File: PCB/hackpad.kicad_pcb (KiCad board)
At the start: 2 copper layers, 67 x 62 mm, 6 parts, among them SW1 SW_Push, SW2 SW_Push, SW3 SW_Push, SW4 SW_Push, U1 MOUDLE-SEEEDUINO-XIAO

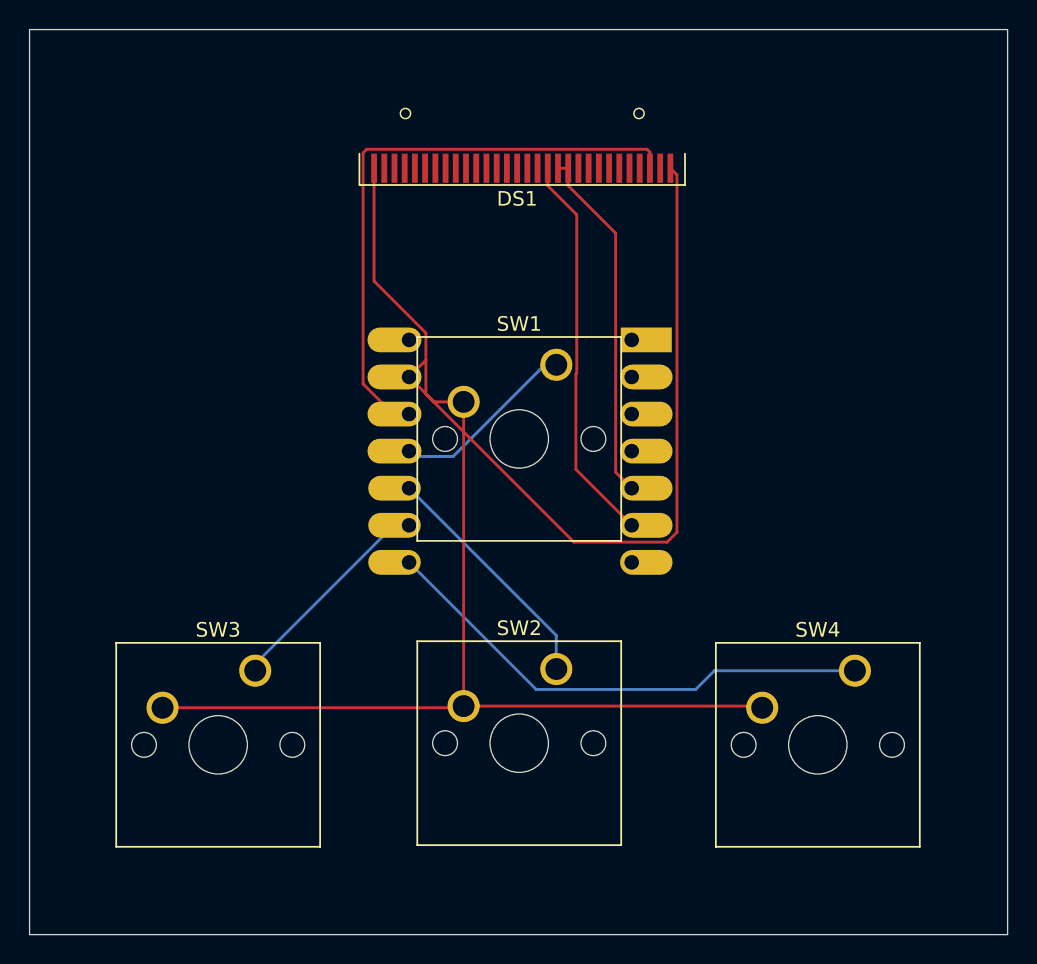
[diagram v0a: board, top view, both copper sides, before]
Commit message: changed oled
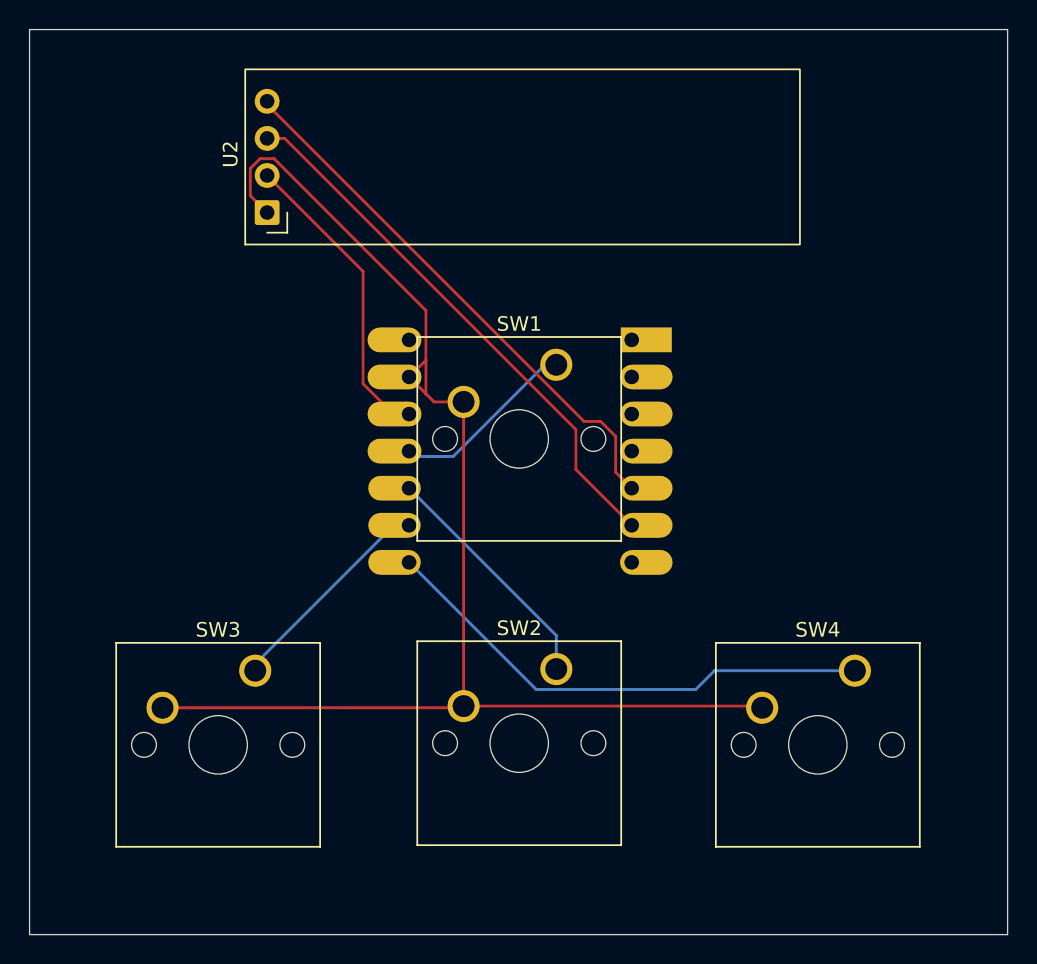
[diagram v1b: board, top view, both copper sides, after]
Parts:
- removed DS1: OLED-128O064D, Display:OLED-128O064D
- added U2: ER_OLEDM0.91_1x-I2C, Display:ER_OLEDM0.91_1x-I2C, F.Cu at (302.8, 387.0)
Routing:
- net GND: track 131.5 -> 93.6 mm
- net Net-(U1-3V3): track 39.7 -> 21.0 mm
- net Net-(U1-PA8_A4_D4_SDA): track 24.4 -> 37.5 mm
- net Net-(U1-PA9_A5_D5_SCL): track 26.9 -> 37.6 mm
